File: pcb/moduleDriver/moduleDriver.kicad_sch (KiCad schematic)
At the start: 54 parts, among them J1 MOTOR, J10 Sensor, J11 Power, J12 Power, J13 Power, J2 MOTOR, J3 MOTOR, J4 MOTOR, J5 IDC, J6 IDC, J7 Sensor, J8 Sensor, J9 Sensor, U1 TPIC6B595, U2 TPIC6B595, U3 74HC165, U4 74HC125, U5 PicoW, U6 OKI-78SR-5_1.5-W36-C, U8 74AHCT125

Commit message: Updated layout
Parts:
- removed H2: MountingHole, MountingHole:MountingHole_3.2mm_M3_ISO7380, symbol Mechanical:MountingHole
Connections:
- net CLOCK_IN: now also U8.11 (4Y); no longer U8.8 (3Y)
- net CLOCK_IN_3V3: now also R4.2, U5.21 (GPIO16), U8.12 (4A); no longer U5.25 (GPIO19), U8.9 (3A)
- net GND: now also U5.42 (GND)
- net LATCH_IN: now also U8.8 (3Y); no longer U8.11 (4Y)
- net LATCH_IN_3V3: now also U5.24 (GPIO18), U8.9 (3A); no longer R12.2, R4.2, U5.22 (GPIO17), U8.12 (4A)
- net MOTOR_IN: now also U8.3 (1Y); no longer U8.6 (2Y)
- net MOTOR_IN_3V3: now also R12.2, U5.26 (GPIO20), U8.2 (1A); no longer U5.24 (GPIO18), U8.5 (2A)
- net SENSOR_OUT_3V3: now also U5.27 (GPIO21); no longer U5.21 (GPIO16)
- net ~{BUFFER_ENABLE_3V3}: now also U5.22 (GPIO17); no longer U5.27 (GPIO21)
- net ~{PWR_ENABLE_IN_3V3}: now also U5.25 (GPIO19), U8.5 (2A); no longer U5.26 (GPIO20), U8.2 (1A)
- net ~{PWR_ENABLE_IN}: now also U8.6 (2Y); no longer U8.3 (1Y)
- net +3.3V: no longer names the net of U5.36 (3V3)

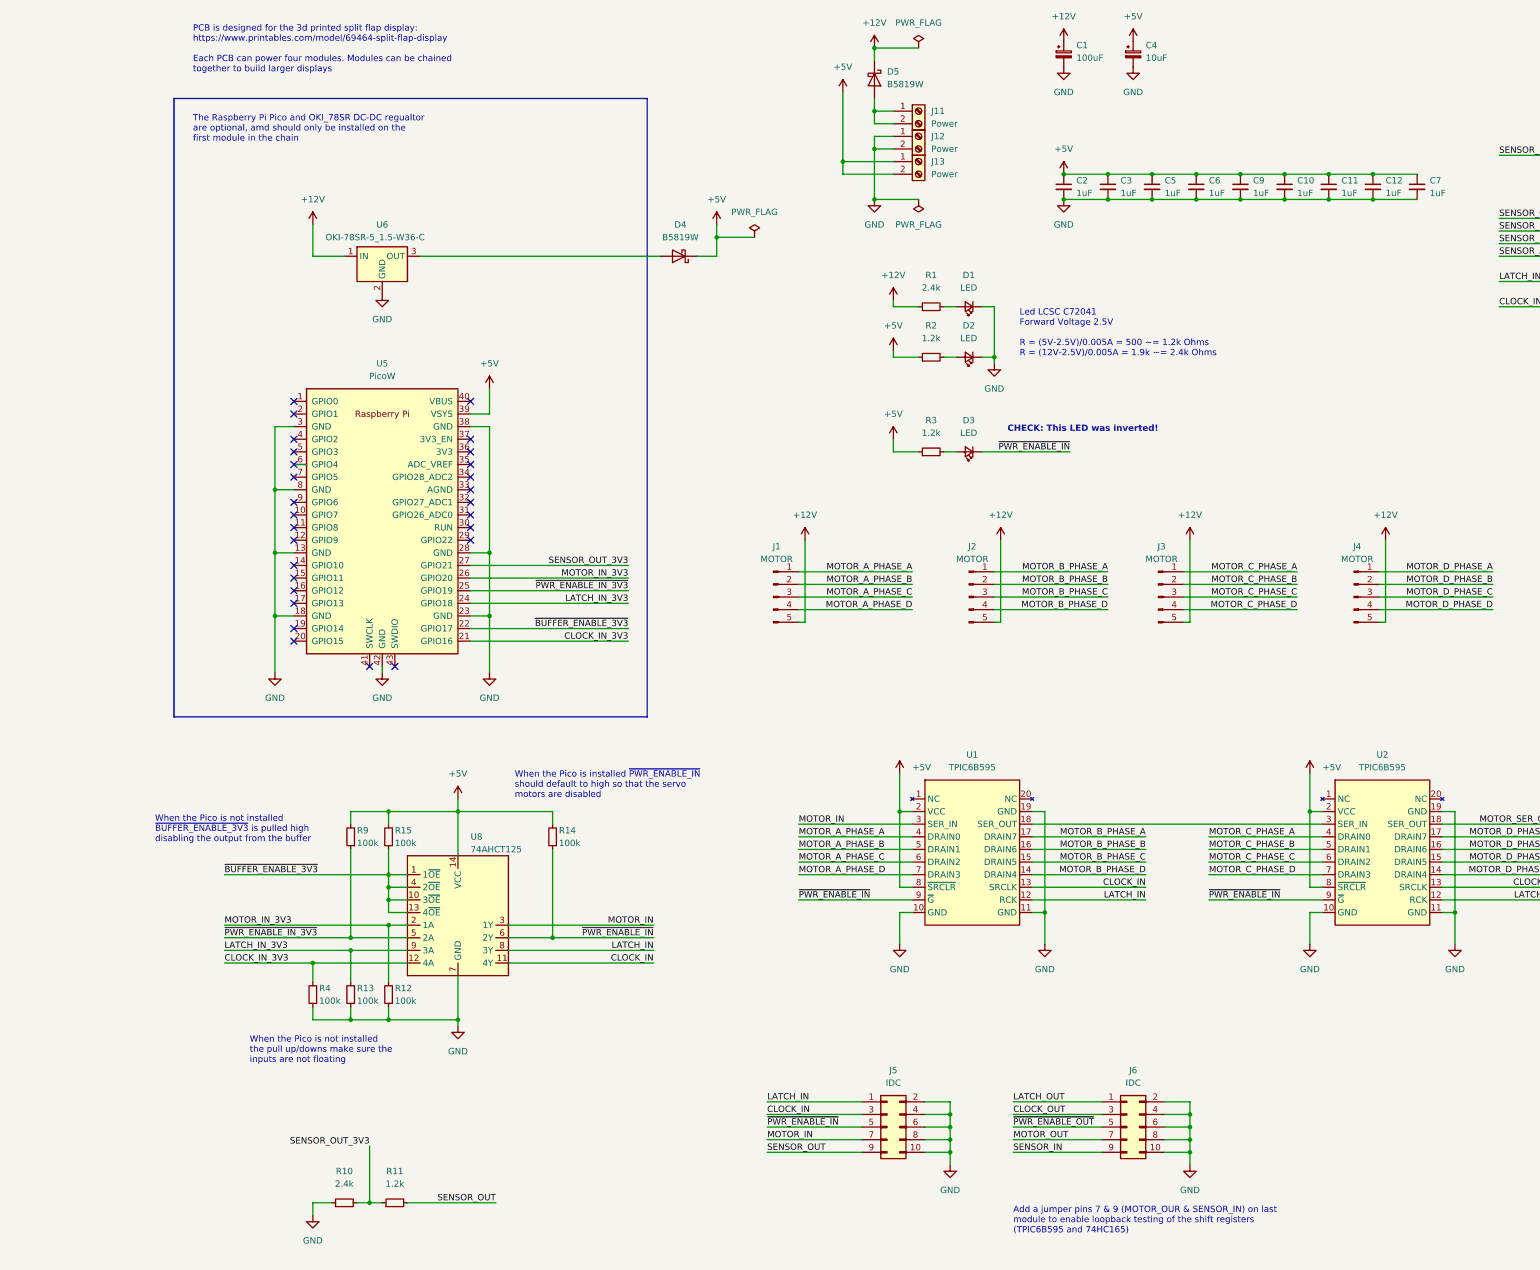
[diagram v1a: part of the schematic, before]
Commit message: Iterate on level translation
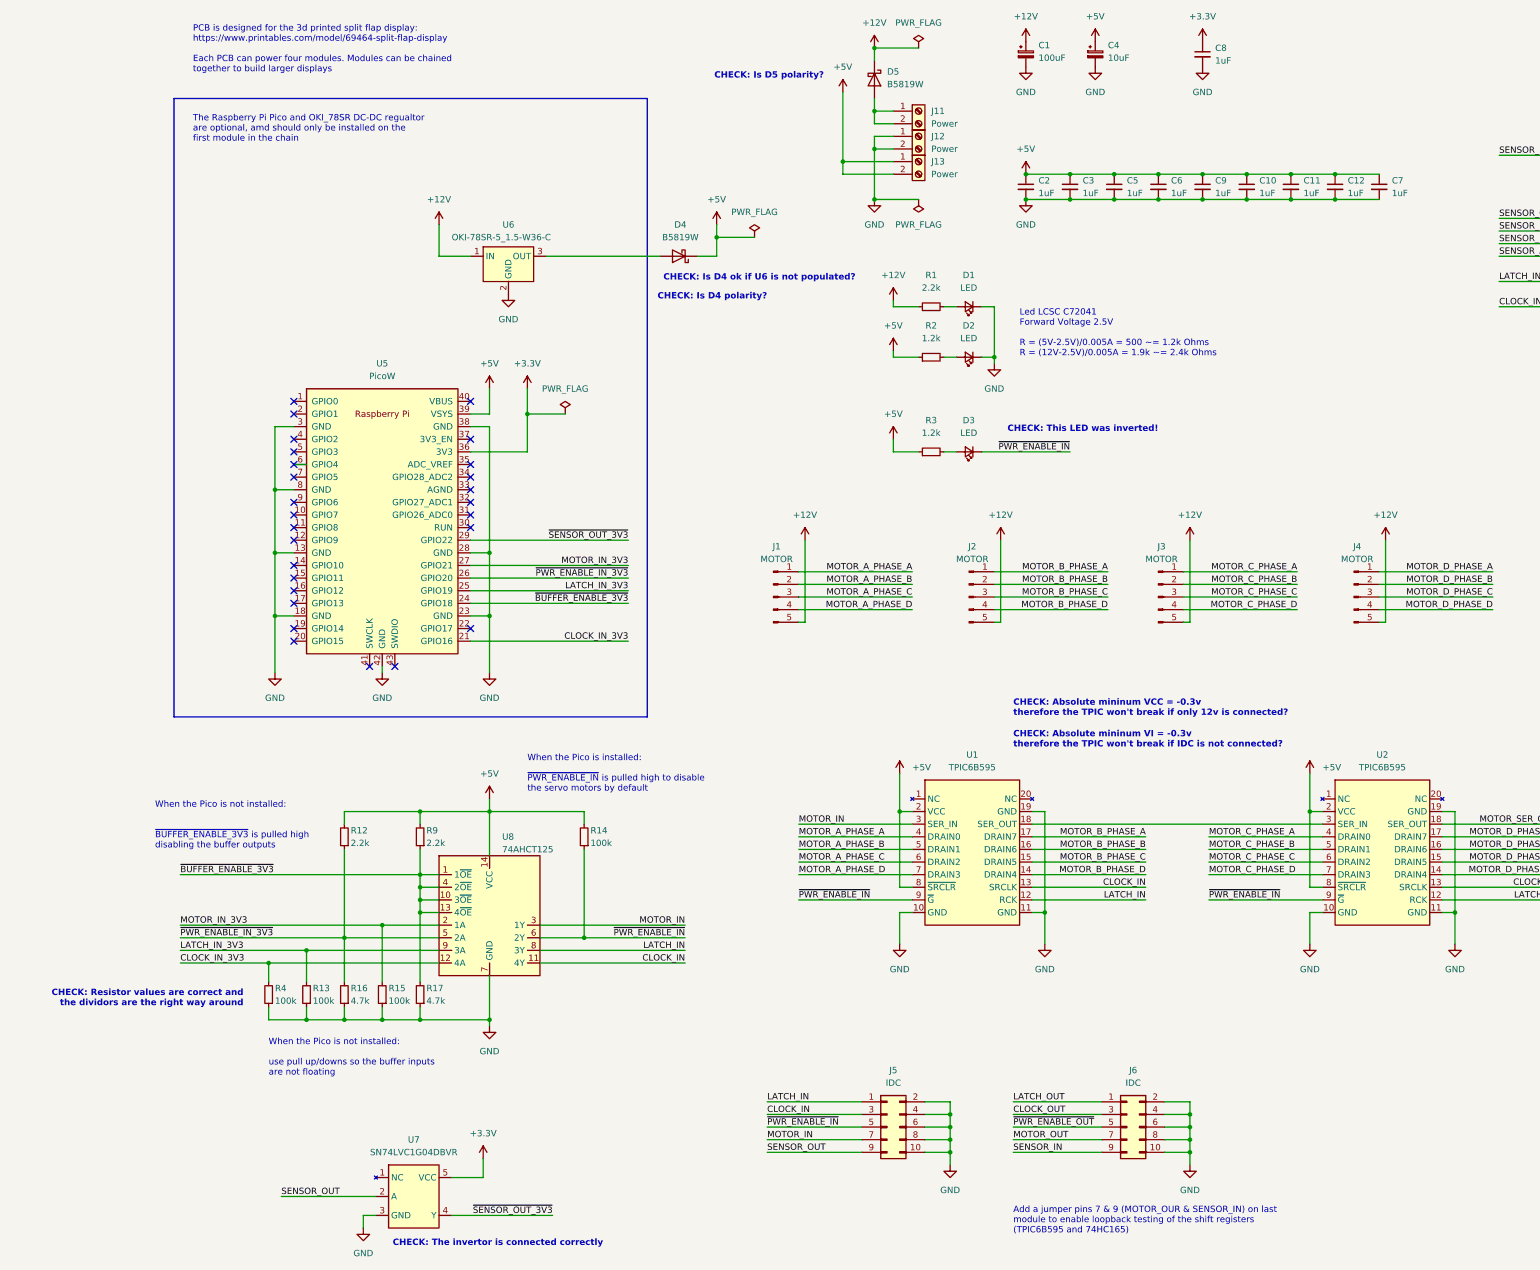
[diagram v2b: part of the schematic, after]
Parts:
- removed R10: 2.4k, Resistor_SMD:R_0603_1608Metric, symbol Device:R_Small
- removed R11: 1.2k, Resistor_SMD:R_0603_1608Metric, symbol Device:R_Small
- added C8: 1uF, Capacitor_SMD:C_0603_1608Metric, symbol Device:C_Small
- added R16, R17: 4.7k, Resistor_SMD:R_0603_1608Metric, symbol Device:R_Small
- added U7: SN74LVC1G04DBVR, Package_TO_SOT_SMD:SOT-23-5, symbol New_Library:SN74LVC1G04DBVR
- R1: value 2.4k -> 2.2k; LCSC# C22940 -> C4190
- R12, R9: value 100k -> 2.2k
- R15: LCSC# C4190 -> C23162
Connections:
- net SENSOR_OUT_3V3 is gone; now on net MOTOR_IN_3V3: U5.27 (GPIO21)
- net +5V: now also R12.2; no longer R15.2
- net GND: now also R15.1, C8.2, R16.1, R17.1, U7.3 (GND); no longer R12.1
- net LATCH_IN_3V3: now also U5.25 (GPIO19); no longer U5.24 (GPIO18)
- net MOTOR_IN_3V3: now also R15.2; no longer R12.2, U5.26 (GPIO20)
- net SENSOR_OUT: now also U7.2 (A)
- net ~{BUFFER_ENABLE_3V3}: now also R9.1, U5.24 (GPIO18), R17.2; no longer R15.1, U5.22 (GPIO17)
- net ~{PWR_ENABLE_IN_3V3}: now also R12.1, U5.26 (GPIO20), R16.2; no longer R9.1, U5.25 (GPIO19)
- net ~{SENSOR_OUT_3V3}: now reaches U5.29 (GPIO22)
- net ~{SENSOR_OUT_3V3}: now also U7.4 (Y)
- net +3.3V: now reaches U5.36 (3V3)
- net +3.3V: now also C8.1, U7.5 (VCC)
- no-connect marks 29 -> 28
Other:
- note added: "CHECK: Absolute mininum VCC = -0.3v therefore the TPIC won't break if only 12v is connected?"
- note added: "CHECK: Absolute mininum VI = -0.3v therefore the TPIC won't break if IDC is not connected?"
- note added: "CHECK: Is D4 ok if U6 is not populated?"
- note added: "CHECK: Is D4 polarity?"
- note added: "CHECK: Is D5 polarity?"
- note added: "CHECK: Resistor values are correct and the dividors are the right way around"
- note added: "CHECK: The invertor is connected correctly"
- note added: "When the Pico is installed: ~{PWR_ENABLE_IN} is pulled high to disable the servo motors by default"
- note added: "When the Pico is not installed: use pull up/downs so the buffer inputs are not floating"
- note added: "When the Pico is not installed: ~{BUFFER_ENABLE_3V3} is pulled high disabling the buffer outputs"
- note removed: "When the Pico is installed ~{PWR_ENABLE_IN} should default to high so that the servo motors are disabled"
- note removed: "When the Pico is not installed the pull up/downs make sure the inputs are not floating"
- note removed: "When the Pico is not installed ~{BUFFER_ENABLE_3V3} is pulled high disabling the output from the buffer"
- moved on the sheet: C1, C10, C11, C12, C2, C3, C4, C5, C6, C7, C9, R12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

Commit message: more modular maybe?
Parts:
- removed D4: B5819W, Diode_SMD:D_SOD-123, symbol Device:D_Schottky
- removed J13: Power, Library:ScrewTerminal-5.08-2P, symbol Connector:Screw_Terminal_01x02
- removed J5, J6: IDC, Connector_IDC:IDC-Header_2x05_P2.54mm_Vertical, symbol Connector_Generic:Conn_02x05_Odd_Even
- removed R12, R9: 2.2k, Resistor_SMD:R_0603_1608Metric, symbol Device:R_Small
- removed R13, R14, R15, R4: 100k, Resistor_SMD:R_0603_1608Metric, symbol Device:R_Small
- removed R16, R17: 4.7k, Resistor_SMD:R_0603_1608Metric, symbol Device:R_Small
- removed U4: 74HC125, Package_SO:SOIC-14_3.9x8.7mm_P1.27mm, symbol New_Library:74HC125
- removed U6: OKI-78SR-5_1.5-W36-C, Converter_DCDC:Converter_DCDC_Murata_OKI-78SR_Vertical, symbol Converter_DCDC:OKI-78SR-5_1.5-W36-C
- added J? (x2): I2C, Connector_PinHeader_2.54mm:PinHeader_1x03_P2.54mm_Vertical, symbol Connector:Conn_01x03_Male
- added R? (x2): 2.2k, Resistor_SMD:R_0603_1608Metric, symbol Device:R_Small
- added R?: 4.7k, Resistor_SMD:R_0603_1608Metric, symbol Device:R_Small
- added SW?: SW_DIP_x01, symbol Switch:SW_DIP_x01
- added U?: MC7805BDTG, Package_TO_SOT_SMD:TO-252-3_TabPin2, symbol Regulator_Linear:L7805
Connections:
- net +12V: now also U?.1 (IN)
- net +3.3V: now also R?.2
- net +5V: now also U8.1 (1~{OE}), U8.10 (3~{OE}), U8.13 (4~{OE}), U8.4 (2~{OE}), U?.3 (OUT)
- net GND: now also U3.3 (D4), U3.4 (D5), U3.5 (D6), U3.6 (D7), J?.1 (Pin_1), J?.1 (Pin_1), SW?.1, U?.2 (GND); no longer U3.11 (D0), U3.12 (D1), U3.13 (D2), U3.14 (D3)
- net SENSOR_A: now also U3.11 (D0); no longer U3.6 (D7)
- net SENSOR_B: now also U3.12 (D1); no longer U3.5 (D6)
- net SENSOR_C: now also U3.13 (D2); no longer U3.3 (D4)
- net SENSOR_D: now also U3.14 (D3); no longer U3.4 (D5)
- net ~{PWR_ENABLE_IN_3V3}: now also R?.1
- net SDA: now reaches U5.31 (GPIO26_ADC0)
- net SDA: now also J?.3 (Pin_3), J?.3 (Pin_3), R?.1
- net SCL: now reaches U5.32 (GPIO27_ADC1)
- net SCL: now also J?.2 (Pin_2), J?.2 (Pin_2), R?.1
- net I2C_PULLUP: now reaches U5.34 (GPIO28_ADC2)
- net I2C_PULLUP: now also R?.2, R?.2
- net at U5.4 (GPIO2): now also SW?.2
- net MOTOR_MODULE2: now reaches U1.18 (SER_OUT), U2.3 (SER_IN)
- net MOTOR_SER_OUT: no longer names the net of U2.18 (SER_OUT)
- net SENSOR_IN: no longer names the net of U3.10 (DS)
- removed net ~{BUFFER_ENABLE_3V3}: U5.24 (GPIO18), U8.1 (1~{OE}), U8.10 (3~{OE}), U8.13 (4~{OE}), U8.4 (2~{OE})
- no-connect marks 28 -> 27
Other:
- note removed: "Add a jumper pins 7 & 9 (MOTOR_OUR & SENSOR_IN) on last module to enable loopback testing of the shift registers (TPIC6B595 and 74HC165)"
- note removed: "CHECK: Absolute mininum VCC = -0.3v therefore the TPIC won't break if only 12v is connected?"
- note removed: "CHECK: Absolute mininum VI = -0.3v therefore the TPIC won't break if IDC is not connected?"
- note removed: "CHECK: Is D4 ok if U6 is not populated?"
- note removed: "CHECK: Is D4 polarity?"
- note removed: "CHECK: Is D5 polarity?"
- note removed: "CHECK: Resistor values are correct and the dividors are the right way around"
- note removed: "CHECK: This LED was inverted!"
- note removed: "Motor data does not need to be buffered for transmission reasons (it is 1:1 from one board to the next, not bussed), but it is buffered to keep timing in sync with the buffered clock. Serial chaining relies on narrow propagation delay > hold time margin to work, so we need to be cognizant of anything that may cause data to change sooner after the rising clock edge (reducing effective propagation 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"
- note removed: "The Raspberry Pi Pico and OKI_78SR DC-DC regualtor are optional, amd should only be installed on the first module in the chain"
- note removed: "When the Pico is installed: ~{PWR_ENABLE_IN} is pulled high to disable the servo motors by default"
- note removed: "When the Pico is not installed: ~{BUFFER_ENABLE_3V3} is pulled high disabling the buffer outputs"
- moved on the sheet: U3, U7

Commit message: oh, this is much more simpler
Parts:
- removed C10, C11, C12, C2, C3, C5, C6, C7, C8, C9: 1uF, Capacitor_SMD:C_0603_1608Metric, symbol Device:C_Small
- removed D1, D2, D3: LED, LED_SMD:LED_0603_1608Metric, symbol Device:LED_Small
- removed R1, R? (x2): 2.2k, Resistor_SMD:R_0603_1608Metric, symbol Device:R_Small
- removed R2, R3: 1.2k, Resistor_SMD:R_0603_1608Metric, symbol Device:R_Small
- removed R?: 4.7k, Resistor_SMD:R_0603_1608Metric, symbol Device:R_Small
- removed SW?: SW_DIP_x01, symbol Switch:SW_DIP_x01
- removed U1, U2: TPIC6B595, Package_SO:SOIC-20W_7.5x12.8mm_P1.27mm, symbol New_Library:TPIC6B595
- removed U3: 74HC165, Package_SO:SOIC-16_3.9x9.9mm_P1.27mm, symbol 74xx:74HC165
- removed U7: SN74LVC1G04DBVR, Package_TO_SOT_SMD:SOT-23-5, symbol New_Library:SN74LVC1G04DBVR
- removed U8: 74AHCT125, Package_SO:TSSOP-14_4.4x5mm_P0.65mm, symbol New_Library:74AHCT125
- added D? (x2): LED, LED_SMD:LED_0603_1608Metric, symbol Device:LED_Small
- added R?: 1.2k, Resistor_SMD:R_0603_1608Metric, symbol Device:R_Small
- added R? (x3): 2.2k, Resistor_SMD:R_0603_1608Metric, symbol Device:R_Small
- added SW?: SW_DIP_x01, symbol Switch:SW_DIP_x01
- added U? (x2): ULN2803A, symbol Transistor_Array:ULN2803A
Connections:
- net LATCH_IN_3V3 is gone; now on net SENSOR_B: U5.25 (GPIO19)
- net MOTOR_IN_3V3 is gone; now on net SDA: U5.27 (GPIO21)
- net ~{PWR_ENABLE_IN_3V3} is gone; now on net SENSOR_A: U5.26 (GPIO20)
- net ~{SENSOR_OUT_3V3} is gone; now on net SCL: U5.29 (GPIO22)
- net +12V: now also R?.1, U?.10 (COM), U?.10 (COM)
- net +3.3V: now also R5.1, R6.1, R7.1, R8.1
- net +5V: no longer R5.1, R6.1, R7.1, R8.1
- net GND: now also D?.1 (K), D?.1 (K), SW?.1, U?.9 (GND), U?.9 (GND)
- net I2C_PULLUP: now also U5.31 (GPIO26_ADC0), R?.2, R?.2; no longer U5.34 (GPIO28_ADC2)
- net MOTOR_A_PHASE_A: now also U?.18 (O1)
- net MOTOR_A_PHASE_B: now also U?.17 (O2)
- net MOTOR_A_PHASE_C: now also U?.16 (O3)
- net MOTOR_A_PHASE_D: now also U?.15 (O4)
- net MOTOR_B_PHASE_A: now also U?.14 (O5)
- net MOTOR_B_PHASE_B: now also U?.13 (O6)
- net MOTOR_B_PHASE_C: now also U?.12 (O7)
- net MOTOR_B_PHASE_D: now also U?.11 (O8)
- net MOTOR_C_PHASE_A: now also U?.18 (O1)
- net MOTOR_C_PHASE_B: now also U?.17 (O2)
- net MOTOR_C_PHASE_C: now also U?.16 (O3)
- net MOTOR_C_PHASE_D: now also U?.15 (O4)
- net MOTOR_D_PHASE_A: now also U?.14 (O5)
- net MOTOR_D_PHASE_B: now also U?.13 (O6)
- net MOTOR_D_PHASE_C: now also U?.12 (O7)
- net MOTOR_D_PHASE_D: now also U?.11 (O8)
- net SCL: now also R?.1; no longer U5.32 (GPIO27_ADC1)
- net SDA: now also R?.1; no longer U5.31 (GPIO26_ADC0)
- net SENSOR_C: now also U5.24 (GPIO18)
- net SENSOR_D: now also U5.22 (GPIO17)
- net MOTOR_A_PHASE_C_P: now reaches U5.4 (GPIO2)
- net MOTOR_A_PHASE_C_P: now also U?.3 (I3)
- net MOTOR_A_PHASE_A_P: now reaches U5.1 (GPIO0)
- net MOTOR_A_PHASE_A_P: now also U?.1 (I1)
- net MOTOR_B_PHASE_D_P: now reaches U5.10 (GPIO7)
- net MOTOR_B_PHASE_D_P: now also U?.8 (I8)
- net MOTOR_C_PHASE_A_P: now reaches U5.11 (GPIO8)
- net MOTOR_C_PHASE_A_P: now also U?.1 (I1)
- net MOTOR_C_PHASE_B_P: now reaches U5.12 (GPIO9)
- net MOTOR_C_PHASE_B_P: now also U?.2 (I2)
- net MOTOR_C_PHASE_C_P: now reaches U5.14 (GPIO10)
- net MOTOR_C_PHASE_C_P: now also U?.3 (I3)
- net MOTOR_C_PHASE_D_P: now reaches U5.15 (GPIO11)
- net MOTOR_C_PHASE_D_P: now also U?.4 (I4)
- net MOTOR_D_PHASE_A_P: now reaches U5.16 (GPIO12)
- net MOTOR_D_PHASE_A_P: now also U?.5 (I5)
- net MOTOR_D_PHASE_B_P: now reaches U5.17 (GPIO13)
- net MOTOR_D_PHASE_B_P: now also U?.6 (I6)
- net MOTOR_D_PHASE_C_P: now reaches U5.19 (GPIO14)
- net MOTOR_D_PHASE_C_P: now also U?.7 (I7)
- net MOTOR_A_PHASE_B_P: now reaches U5.2 (GPIO1)
- net MOTOR_A_PHASE_B_P: now also U?.2 (I2)
- net MOTOR_D_PHASE_D_P: now reaches U5.20 (GPIO15)
- net MOTOR_D_PHASE_D_P: now also U?.8 (I8)
- net MOTOR_A_PHASE_D_P: now reaches U5.5 (GPIO3)
- net MOTOR_A_PHASE_D_P: now also U?.4 (I4)
- net MOTOR_B_PHASE_A_P: now reaches U5.6 (GPIO4)
- net MOTOR_B_PHASE_A_P: now also U?.5 (I5)
- net MOTOR_B_PHASE_B_P: now reaches U5.7 (GPIO5)
- net MOTOR_B_PHASE_B_P: now also U?.6 (I6)
- net MOTOR_B_PHASE_C_P: now reaches U5.9 (GPIO6)
- net MOTOR_B_PHASE_C_P: now also U?.7 (I7)
- net CLOCK_IN_3V3: no longer names the net of U5.21 (GPIO16)
- net CLOCK_IN_3V3: now also R?.1
- new net: D?.2 (A), R?.2 (x2)
- new net: SW?.2, U5.34 (GPIO28_ADC2)
- no-connect marks 27 -> 25
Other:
- note added: "HALL EFFECT SENSORS"
- note added: "I2C to other modules"
- note added: "MOTOR DRIVERS"
- note added: "PICO"
- note added: "POWER SUPPLIES"
- note removed: "CHECK: The invertor is connected correctly"
- note removed: "Led LCSC C72041 Forward Voltage 2.5V R = (5V-2.5V)/0.005A = 500 ~= 1.2k Ohms R = (12V-2.5V)/0.005A = 1.9k ~= 2.4k Ohms"
- note removed: "When the Pico is not installed: use pull up/downs so the buffer inputs are not floating"
- moved on the sheet: C1, C4, D5, H1, H3, J1, J10, J11, J12, J2, J3, J4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
